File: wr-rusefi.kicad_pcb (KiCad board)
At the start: 2 copper layers, 94 x 94 mm, 147 parts, among them P101 USB_OTG, P102 CONN_01X08, P103 CONN_01X08, P104 CONN_01X04, P105 CONN_01X08, P106 CONN_01X08, P107 CONN_01X02, P108 USB_OTG, P109 CONN_01X02, P110 CONN_01X06, Q401 IRF540N, Q402 IRF540N, Q403 IRF540N, Q404 IRF540N, Q405 IRF540N, Q406 IRF540N, U101 ISL89410, U102 ISL89410, U103 FT230XS, U104 MAX9924, U105 MCP2562-E/SN, U106 LD1117S33TR, U107 MAX9924, U108 ISL89410, U109 STM32F407VGTx, U110 ISL89410, U201 LM324, U301 LM324, U501 LM7805CT, Y101 Crystal

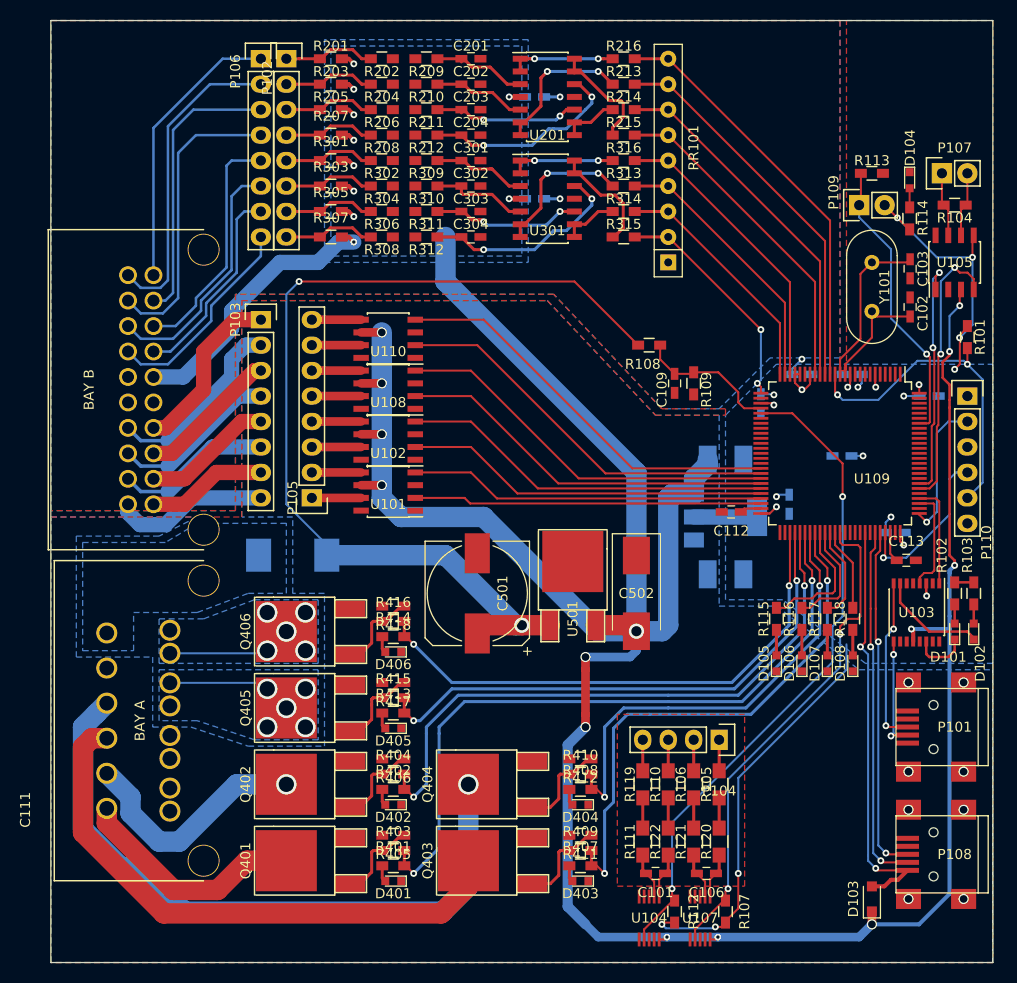
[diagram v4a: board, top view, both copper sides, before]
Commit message: Via stitching bonanza
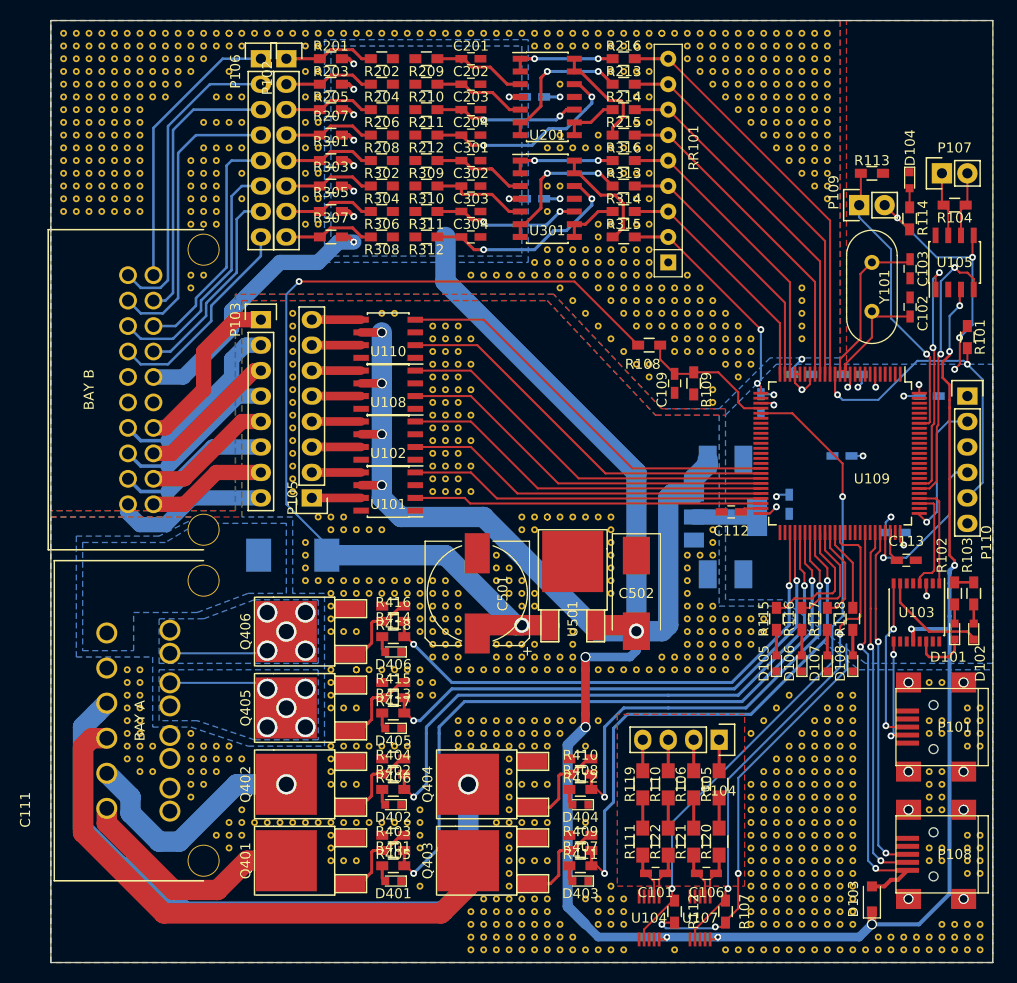
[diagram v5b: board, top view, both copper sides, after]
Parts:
- added REF**: via-stitch, wr-efi:via-stitch, F.Cu at (67.3, 132.1)
- added REF**: via-stitch, wr-efi:via-stitch, F.Cu at (139.7, 141.0)
- added REF**: via-stitch, wr-efi:via-stitch, F.Cu at (77.5, 55.9)
- added REF**: via-stitch, wr-efi:via-stitch, F.Cu at (62.2, 58.4)
- added REF**: via-stitch, wr-efi:via-stitch, F.Cu at (61.0, 52.1)
- added REF**: via-stitch, wr-efi:via-stitch, F.Cu at (61.0, 53.3)
- added REF**: via-stitch, wr-efi:via-stitch, F.Cu at (61.0, 54.6)
- added REF**: via-stitch, wr-efi:via-stitch, F.Cu at (61.0, 55.9)
- added REF**: via-stitch, wr-efi:via-stitch, F.Cu at (61.0, 57.1)
- added REF**: via-stitch, wr-efi:via-stitch, F.Cu at (61.0, 58.4)
- added REF**: via-stitch, wr-efi:via-stitch, F.Cu at (59.7, 69.8)
- added REF**: via-stitch, wr-efi:via-stitch, F.Cu at (58.4, 69.8)
- added REF**: via-stitch, wr-efi:via-stitch, F.Cu at (57.1, 69.8)
- added REF**: via-stitch, wr-efi:via-stitch, F.Cu at (77.5, 58.4)
- added REF**: via-stitch, wr-efi:via-stitch, F.Cu at (55.9, 69.8)
- added REF**: via-stitch, wr-efi:via-stitch, F.Cu at (54.6, 69.8)
- added REF**: via-stitch, wr-efi:via-stitch, F.Cu at (53.3, 69.8)
- added REF**: via-stitch, wr-efi:via-stitch, F.Cu at (52.1, 69.8)
- added REF**: via-stitch, wr-efi:via-stitch, F.Cu at (59.7, 68.6)
- added REF**: via-stitch, wr-efi:via-stitch, F.Cu at (58.4, 68.6)
- added REF**: via-stitch, wr-efi:via-stitch, F.Cu at (57.1, 68.6)
- added REF**: via-stitch, wr-efi:via-stitch, F.Cu at (55.9, 68.6)
- added REF**: via-stitch, wr-efi:via-stitch, F.Cu at (54.6, 68.6)
- added REF**: via-stitch, wr-efi:via-stitch, F.Cu at (53.3, 68.6)
- added REF**: via-stitch, wr-efi:via-stitch, F.Cu at (76.2, 58.4)
- added REF**: via-stitch, wr-efi:via-stitch, F.Cu at (52.1, 68.6)
- added REF**: via-stitch, wr-efi:via-stitch, F.Cu at (59.7, 67.3)
- added REF**: via-stitch, wr-efi:via-stitch, F.Cu at (58.4, 67.3)
- added REF**: via-stitch, wr-efi:via-stitch, F.Cu at (57.1, 67.3)
- added REF**: via-stitch, wr-efi:via-stitch, F.Cu at (55.9, 67.3)
- added REF**: via-stitch, wr-efi:via-stitch, F.Cu at (54.6, 67.3)
- added REF**: via-stitch, wr-efi:via-stitch, F.Cu at (53.3, 67.3)
- added REF**: via-stitch, wr-efi:via-stitch, F.Cu at (52.1, 67.3)
- added REF**: via-stitch, wr-efi:via-stitch, F.Cu at (59.7, 66.0)
- added REF**: via-stitch, wr-efi:via-stitch, F.Cu at (58.4, 66.0)
- added REF**: via-stitch, wr-efi:via-stitch, F.Cu at (76.2, 61.0)
- added REF**: via-stitch, wr-efi:via-stitch, F.Cu at (57.1, 66.0)
- added REF**: via-stitch, wr-efi:via-stitch, F.Cu at (55.9, 66.0)
- added REF**: via-stitch, wr-efi:via-stitch, F.Cu at (54.6, 66.0)
- added REF**: via-stitch, wr-efi:via-stitch, F.Cu at (53.3, 66.0)
- added REF**: via-stitch, wr-efi:via-stitch, F.Cu at (52.1, 66.0)
- added REF**: via-stitch, wr-efi:via-stitch, F.Cu at (59.7, 64.8)
- added REF**: via-stitch, wr-efi:via-stitch, F.Cu at (58.4, 64.8)
- added REF**: via-stitch, wr-efi:via-stitch, F.Cu at (57.1, 64.8)
- added REF**: via-stitch, wr-efi:via-stitch, F.Cu at (55.9, 64.8)
- added REF**: via-stitch, wr-efi:via-stitch, F.Cu at (54.6, 64.8)
- added REF**: via-stitch, wr-efi:via-stitch, F.Cu at (77.5, 61.0)
- added REF**: via-stitch, wr-efi:via-stitch, F.Cu at (53.3, 64.8)
- added REF**: via-stitch, wr-efi:via-stitch, F.Cu at (52.1, 64.8)
- added REF**: via-stitch, wr-efi:via-stitch, F.Cu at (59.7, 63.5)
- added REF**: via-stitch, wr-efi:via-stitch, F.Cu at (58.4, 63.5)
- added REF**: via-stitch, wr-efi:via-stitch, F.Cu at (57.1, 63.5)
- added REF**: via-stitch, wr-efi:via-stitch, F.Cu at (55.9, 63.5)
- added REF**: via-stitch, wr-efi:via-stitch, F.Cu at (54.6, 63.5)
- added REF**: via-stitch, wr-efi:via-stitch, F.Cu at (53.3, 63.5)
- added REF**: via-stitch, wr-efi:via-stitch, F.Cu at (52.1, 63.5)
- added REF**: via-stitch, wr-efi:via-stitch, F.Cu at (59.7, 62.2)
- added REF**: via-stitch, wr-efi:via-stitch, F.Cu at (77.5, 63.5)
- added REF**: via-stitch, wr-efi:via-stitch, F.Cu at (58.4, 62.2)
- added REF**: via-stitch, wr-efi:via-stitch, F.Cu at (57.1, 62.2)
- added REF**: via-stitch, wr-efi:via-stitch, F.Cu at (55.9, 62.2)
- added REF**: via-stitch, wr-efi:via-stitch, F.Cu at (54.6, 62.2)
- added REF**: via-stitch, wr-efi:via-stitch, F.Cu at (53.3, 62.2)
- added REF**: via-stitch, wr-efi:via-stitch, F.Cu at (52.1, 62.2)
- added REF**: via-stitch, wr-efi:via-stitch, F.Cu at (59.7, 61.0)
- added REF**: via-stitch, wr-efi:via-stitch, F.Cu at (58.4, 61.0)
- added REF**: via-stitch, wr-efi:via-stitch, F.Cu at (57.1, 61.0)
- added REF**: via-stitch, wr-efi:via-stitch, F.Cu at (55.9, 61.0)
- added REF**: via-stitch, wr-efi:via-stitch, F.Cu at (76.2, 63.5)
- added REF**: via-stitch, wr-efi:via-stitch, F.Cu at (54.6, 61.0)
- added REF**: via-stitch, wr-efi:via-stitch, F.Cu at (53.3, 61.0)
- added REF**: via-stitch, wr-efi:via-stitch, F.Cu at (52.1, 61.0)
- added REF**: via-stitch, wr-efi:via-stitch, F.Cu at (59.7, 59.7)
- added REF**: via-stitch, wr-efi:via-stitch, F.Cu at (58.4, 59.7)
- added REF**: via-stitch, wr-efi:via-stitch, F.Cu at (57.1, 59.7)
- added REF**: via-stitch, wr-efi:via-stitch, F.Cu at (55.9, 59.7)
- added REF**: via-stitch, wr-efi:via-stitch, F.Cu at (54.6, 59.7)
- added REF**: via-stitch, wr-efi:via-stitch, F.Cu at (53.3, 59.7)
- added REF**: via-stitch, wr-efi:via-stitch, F.Cu at (52.1, 59.7)
- added REF**: via-stitch, wr-efi:via-stitch, F.Cu at (77.5, 66.0)
- added REF**: via-stitch, wr-efi:via-stitch, F.Cu at (59.7, 58.4)
- added REF**: via-stitch, wr-efi:via-stitch, F.Cu at (58.4, 58.4)
- added REF**: via-stitch, wr-efi:via-stitch, F.Cu at (57.1, 58.4)
- added REF**: via-stitch, wr-efi:via-stitch, F.Cu at (55.9, 58.4)
- added REF**: via-stitch, wr-efi:via-stitch, F.Cu at (54.6, 58.4)
- added REF**: via-stitch, wr-efi:via-stitch, F.Cu at (53.3, 58.4)
- added REF**: via-stitch, wr-efi:via-stitch, F.Cu at (52.1, 58.4)
- added REF**: via-stitch, wr-efi:via-stitch, F.Cu at (59.7, 57.1)
- added REF**: via-stitch, wr-efi:via-stitch, F.Cu at (58.4, 57.1)
- added REF**: via-stitch, wr-efi:via-stitch, F.Cu at (57.1, 57.1)
- added REF**: via-stitch, wr-efi:via-stitch, F.Cu at (76.2, 66.0)
- added REF**: via-stitch, wr-efi:via-stitch, F.Cu at (55.9, 57.1)
- added REF**: via-stitch, wr-efi:via-stitch, F.Cu at (54.6, 57.1)
- added REF**: via-stitch, wr-efi:via-stitch, F.Cu at (53.3, 57.1)
- added REF**: via-stitch, wr-efi:via-stitch, F.Cu at (52.1, 57.1)
- added REF**: via-stitch, wr-efi:via-stitch, F.Cu at (59.7, 55.9)
- added REF**: via-stitch, wr-efi:via-stitch, F.Cu at (58.4, 55.9)
- added REF**: via-stitch, wr-efi:via-stitch, F.Cu at (57.1, 55.9)
- added REF**: via-stitch, wr-efi:via-stitch, F.Cu at (55.9, 55.9)
- added REF**: via-stitch, wr-efi:via-stitch, F.Cu at (54.6, 55.9)
- added REF**: via-stitch, wr-efi:via-stitch, F.Cu at (53.3, 55.9)
- added REF**: via-stitch, wr-efi:via-stitch, F.Cu at (76.2, 68.6)
- added REF**: via-stitch, wr-efi:via-stitch, F.Cu at (52.1, 55.9)
- added REF**: via-stitch, wr-efi:via-stitch, F.Cu at (59.7, 54.6)
- added REF**: via-stitch, wr-efi:via-stitch, F.Cu at (58.4, 54.6)
- added REF**: via-stitch, wr-efi:via-stitch, F.Cu at (57.1, 54.6)
- added REF**: via-stitch, wr-efi:via-stitch, F.Cu at (55.9, 54.6)
- added REF**: via-stitch, wr-efi:via-stitch, F.Cu at (54.6, 54.6)
- added REF**: via-stitch, wr-efi:via-stitch, F.Cu at (53.3, 54.6)
- added REF**: via-stitch, wr-efi:via-stitch, F.Cu at (52.1, 54.6)
- added REF**: via-stitch, wr-efi:via-stitch, F.Cu at (59.7, 53.3)
- added REF**: via-stitch, wr-efi:via-stitch, F.Cu at (58.4, 53.3)
- added REF**: via-stitch, wr-efi:via-stitch, F.Cu at (143.5, 141.0)
- added REF**: via-stitch, wr-efi:via-stitch, F.Cu at (77.5, 68.6)
- added REF**: via-stitch, wr-efi:via-stitch, F.Cu at (57.1, 53.3)
- added REF**: via-stitch, wr-efi:via-stitch, F.Cu at (55.9, 53.3)
- added REF**: via-stitch, wr-efi:via-stitch, F.Cu at (54.6, 53.3)
- added REF**: via-stitch, wr-efi:via-stitch, F.Cu at (53.3, 53.3)
- added REF**: via-stitch, wr-efi:via-stitch, F.Cu at (52.1, 53.3)
- added REF**: via-stitch, wr-efi:via-stitch, F.Cu at (59.7, 52.1)
- added REF**: via-stitch, wr-efi:via-stitch, F.Cu at (58.4, 52.1)
- added REF**: via-stitch, wr-efi:via-stitch, F.Cu at (57.1, 52.1)
- added REF**: via-stitch, wr-efi:via-stitch, F.Cu at (55.9, 52.1)
- added REF**: via-stitch, wr-efi:via-stitch, F.Cu at (54.6, 52.1)
- added REF**: via-stitch, wr-efi:via-stitch, F.Cu at (77.5, 71.1)
- added REF**: via-stitch, wr-efi:via-stitch, F.Cu at (53.3, 52.1)
- added REF**: via-stitch, wr-efi:via-stitch, F.Cu at (52.1, 52.1)
- added REF**: via-stitch, wr-efi:via-stitch, F.Cu at (76.2, 71.1)
- added REF**: via-stitch, wr-efi:via-stitch, F.Cu at (67.3, 71.1)
- added REF**: via-stitch, wr-efi:via-stitch, F.Cu at (66.0, 71.1)
- added REF**: via-stitch, wr-efi:via-stitch, F.Cu at (64.8, 71.1)
- added REF**: via-stitch, wr-efi:via-stitch, F.Cu at (69.8, 129.5)
- added REF**: via-stitch, wr-efi:via-stitch, F.Cu at (68.6, 130.8)
- added REF**: via-stitch, wr-efi:via-stitch, F.Cu at (61.0, 123.2)
- added REF**: via-stitch, wr-efi:via-stitch, F.Cu at (61.0, 125.7)
- added REF**: via-stitch, wr-efi:via-stitch, F.Cu at (143.5, 142.2)
- added REF**: via-stitch, wr-efi:via-stitch, F.Cu at (64.8, 121.9)
- added REF**: via-stitch, wr-efi:via-stitch, F.Cu at (78.7, 101.6)
- added REF**: via-stitch, wr-efi:via-stitch, F.Cu at (77.5, 100.3)
- added REF**: via-stitch, wr-efi:via-stitch, F.Cu at (74.9, 97.8)
- added REF**: via-stitch, wr-efi:via-stitch, F.Cu at (74.9, 96.5)
- added REF**: via-stitch, wr-efi:via-stitch, F.Cu at (74.9, 95.2)
- added REF**: via-stitch, wr-efi:via-stitch, F.Cu at (74.9, 94.0)
- added REF**: via-stitch, wr-efi:via-stitch, F.Cu at (74.9, 92.7)
- added REF**: via-stitch, wr-efi:via-stitch, F.Cu at (74.9, 91.4)
- added REF**: via-stitch, wr-efi:via-stitch, F.Cu at (74.9, 90.2)
- added REF**: via-stitch, wr-efi:via-stitch, F.Cu at (143.5, 143.5)
- added REF**: via-stitch, wr-efi:via-stitch, F.Cu at (74.9, 88.9)
- added REF**: via-stitch, wr-efi:via-stitch, F.Cu at (74.9, 87.6)
- added REF**: via-stitch, wr-efi:via-stitch, F.Cu at (74.9, 86.4)
- added REF**: via-stitch, wr-efi:via-stitch, F.Cu at (74.9, 85.1)
- added REF**: via-stitch, wr-efi:via-stitch, F.Cu at (74.9, 83.8)
- added REF**: via-stitch, wr-efi:via-stitch, F.Cu at (74.9, 82.5)
- added REF**: via-stitch, wr-efi:via-stitch, F.Cu at (83.8, 80.0)
- added REF**: via-stitch, wr-efi:via-stitch, F.Cu at (85.1, 80.0)
- added REF**: via-stitch, wr-efi:via-stitch, F.Cu at (125.7, 77.5)
- added REF**: via-stitch, wr-efi:via-stitch, F.Cu at (125.7, 78.7)
- added REF**: via-stitch, wr-efi:via-stitch, F.Cu at (139.7, 143.5)
- added REF**: via-stitch, wr-efi:via-stitch, F.Cu at (125.7, 80.0)
- added REF**: via-stitch, wr-efi:via-stitch, F.Cu at (125.7, 81.3)
- added REF**: via-stitch, wr-efi:via-stitch, F.Cu at (125.7, 82.5)
- added REF**: via-stitch, wr-efi:via-stitch, F.Cu at (64.8, 77.5)
- added REF**: via-stitch, wr-efi:via-stitch, F.Cu at (64.8, 76.2)
- added REF**: via-stitch, wr-efi:via-stitch, F.Cu at (68.6, 55.9)
- added REF**: via-stitch, wr-efi:via-stitch, F.Cu at (67.3, 58.4)
- added REF**: via-stitch, wr-efi:via-stitch, F.Cu at (68.6, 58.4)
- added REF**: via-stitch, wr-efi:via-stitch, F.Cu at (69.8, 58.4)
- added REF**: via-stitch, wr-efi:via-stitch, F.Cu at (69.8, 68.6)
- added REF**: via-stitch, wr-efi:via-stitch, F.Cu at (141.0, 143.5)
- added REF**: via-stitch, wr-efi:via-stitch, F.Cu at (69.8, 66.0)
- added REF**: via-stitch, wr-efi:via-stitch, F.Cu at (66.0, 66.0)
- added REF**: via-stitch, wr-efi:via-stitch, F.Cu at (67.3, 66.0)
- added REF**: via-stitch, wr-efi:via-stitch, F.Cu at (67.3, 67.3)
- added REF**: via-stitch, wr-efi:via-stitch, F.Cu at (66.0, 67.3)
- added REF**: via-stitch, wr-efi:via-stitch, F.Cu at (66.0, 68.6)
- added REF**: via-stitch, wr-efi:via-stitch, F.Cu at (67.3, 68.6)
- added REF**: via-stitch, wr-efi:via-stitch, F.Cu at (67.3, 69.8)
- added REF**: via-stitch, wr-efi:via-stitch, F.Cu at (66.0, 69.8)
- added REF**: via-stitch, wr-efi:via-stitch, F.Cu at (64.8, 69.8)
- added REF**: via-stitch, wr-efi:via-stitch, F.Cu at (142.2, 143.5)
- added REF**: via-stitch, wr-efi:via-stitch, F.Cu at (64.8, 68.6)
- added REF**: via-stitch, wr-efi:via-stitch, F.Cu at (64.8, 67.3)
- added REF**: via-stitch, wr-efi:via-stitch, F.Cu at (64.8, 66.0)
- added REF**: via-stitch, wr-efi:via-stitch, F.Cu at (67.3, 64.8)
- added REF**: via-stitch, wr-efi:via-stitch, F.Cu at (66.0, 64.8)
- added REF**: via-stitch, wr-efi:via-stitch, F.Cu at (64.8, 64.8)
- added REF**: via-stitch, wr-efi:via-stitch, F.Cu at (66.0, 63.5)
- added REF**: via-stitch, wr-efi:via-stitch, F.Cu at (67.3, 63.5)
- added REF**: via-stitch, wr-efi:via-stitch, F.Cu at (68.6, 63.5)
- added REF**: via-stitch, wr-efi:via-stitch, F.Cu at (67.3, 61.0)
- added REF**: via-stitch, wr-efi:via-stitch, F.Cu at (137.2, 143.5)
- added REF**: via-stitch, wr-efi:via-stitch, F.Cu at (66.0, 61.0)
- added REF**: via-stitch, wr-efi:via-stitch, F.Cu at (68.6, 61.0)
- added REF**: via-stitch, wr-efi:via-stitch, F.Cu at (69.8, 61.0)
- added REF**: via-stitch, wr-efi:via-stitch, F.Cu at (69.8, 63.5)
- added REF**: via-stitch, wr-efi:via-stitch, F.Cu at (101.6, 62.2)
- added REF**: via-stitch, wr-efi:via-stitch, F.Cu at (101.6, 57.1)
- added REF**: via-stitch, wr-efi:via-stitch, F.Cu at (100.3, 69.8)
- added REF**: via-stitch, wr-efi:via-stitch, F.Cu at (100.3, 67.3)
- added REF**: via-stitch, wr-efi:via-stitch, F.Cu at (101.6, 67.3)
- added REF**: via-stitch, wr-efi:via-stitch, F.Cu at (105.4, 72.4)
- added REF**: via-stitch, wr-efi:via-stitch, F.Cu at (138.4, 143.5)
- added REF**: via-stitch, wr-efi:via-stitch, F.Cu at (105.4, 71.1)
- added REF**: via-stitch, wr-efi:via-stitch, F.Cu at (106.7, 71.1)
- added REF**: via-stitch, wr-efi:via-stitch, F.Cu at (109.2, 71.1)
- added REF**: via-stitch, wr-efi:via-stitch, F.Cu at (110.5, 71.1)
- added REF**: via-stitch, wr-efi:via-stitch, F.Cu at (109.2, 68.6)
- added REF**: via-stitch, wr-efi:via-stitch, F.Cu at (110.5, 68.6)
- added REF**: via-stitch, wr-efi:via-stitch, F.Cu at (110.5, 66.0)
- added REF**: via-stitch, wr-efi:via-stitch, F.Cu at (109.2, 66.0)
- added REF**: via-stitch, wr-efi:via-stitch, F.Cu at (108.0, 66.0)
- added REF**: via-stitch, wr-efi:via-stitch, F.Cu at (106.7, 66.0)
- added REF**: via-stitch, wr-efi:via-stitch, F.Cu at (135.9, 143.5)
- added REF**: via-stitch, wr-efi:via-stitch, F.Cu at (106.7, 55.9)
- added REF**: via-stitch, wr-efi:via-stitch, F.Cu at (108.0, 55.9)
- added REF**: via-stitch, wr-efi:via-stitch, F.Cu at (109.2, 55.9)
- added REF**: via-stitch, wr-efi:via-stitch, F.Cu at (110.5, 55.9)
- added REF**: via-stitch, wr-efi:via-stitch, F.Cu at (110.5, 58.4)
- added REF**: via-stitch, wr-efi:via-stitch, F.Cu at (109.2, 58.4)
- added REF**: via-stitch, wr-efi:via-stitch, F.Cu at (109.2, 61.0)
- added REF**: via-stitch, wr-efi:via-stitch, F.Cu at (110.5, 61.0)
- added REF**: via-stitch, wr-efi:via-stitch, F.Cu at (110.5, 63.5)
- added REF**: via-stitch, wr-efi:via-stitch, F.Cu at (109.2, 63.5)
- added REF**: via-stitch, wr-efi:via-stitch, F.Cu at (66.0, 76.2)
- added REF**: via-stitch, wr-efi:via-stitch, F.Cu at (134.6, 143.5)
- added REF**: via-stitch, wr-efi:via-stitch, F.Cu at (108.0, 63.5)
- added REF**: via-stitch, wr-efi:via-stitch, F.Cu at (106.7, 63.5)
- added REF**: via-stitch, wr-efi:via-stitch, F.Cu at (105.4, 62.2)
- added REF**: via-stitch, wr-efi:via-stitch, F.Cu at (105.4, 63.5)
- added REF**: via-stitch, wr-efi:via-stitch, F.Cu at (104.1, 63.5)
- added REF**: via-stitch, wr-efi:via-stitch, F.Cu at (102.9, 63.5)
- added REF**: via-stitch, wr-efi:via-stitch, F.Cu at (101.6, 63.5)
- added REF**: via-stitch, wr-efi:via-stitch, F.Cu at (100.3, 63.5)
- added REF**: via-stitch, wr-efi:via-stitch, F.Cu at (69.8, 53.3)
- added REF**: via-stitch, wr-efi:via-stitch, F.Cu at (77.5, 53.3)
- added REF**: via-stitch, wr-efi:via-stitch, F.Cu at (133.3, 143.5)
- added REF**: via-stitch, wr-efi:via-stitch, F.Cu at (76.2, 53.3)
- added REF**: via-stitch, wr-efi:via-stitch, F.Cu at (97.8, 52.1)
- added REF**: via-stitch, wr-efi:via-stitch, F.Cu at (96.5, 52.1)
- added REF**: via-stitch, wr-efi:via-stitch, F.Cu at (95.2, 52.1)
- added REF**: via-stitch, wr-efi:via-stitch, F.Cu at (94.0, 52.1)
- added REF**: via-stitch, wr-efi:via-stitch, F.Cu at (92.7, 52.1)
- added REF**: via-stitch, wr-efi:via-stitch, F.Cu at (91.4, 52.1)
- added REF**: via-stitch, wr-efi:via-stitch, F.Cu at (90.2, 52.1)
- added REF**: via-stitch, wr-efi:via-stitch, F.Cu at (88.9, 52.1)
- added REF**: via-stitch, wr-efi:via-stitch, F.Cu at (87.6, 52.1)
- added REF**: via-stitch, wr-efi:via-stitch, F.Cu at (132.1, 143.5)
- added REF**: via-stitch, wr-efi:via-stitch, F.Cu at (86.4, 52.1)
- added REF**: via-stitch, wr-efi:via-stitch, F.Cu at (85.1, 52.1)
- added REF**: via-stitch, wr-efi:via-stitch, F.Cu at (83.8, 52.1)
- added REF**: via-stitch, wr-efi:via-stitch, F.Cu at (82.5, 52.1)
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
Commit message: more vias
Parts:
- added REF**: via-stitch, wr-efi:via-stitch, F.Cu at (105.4, 137.2)
- added REF**: via-stitch, wr-efi:via-stitch, F.Cu at (111.8, 88.9)
- added REF**: via-stitch, wr-efi:via-stitch, F.Cu at (113.0, 91.4)
- added REF**: via-stitch, wr-efi:via-stitch, F.Cu at (111.8, 91.4)
- added REF**: via-stitch, wr-efi:via-stitch, F.Cu at (111.8, 92.7)
- added REF**: via-stitch, wr-efi:via-stitch, F.Cu at (106.7, 90.2)
- added REF**: via-stitch, wr-efi:via-stitch, F.Cu at (105.4, 88.9)
- added REF**: via-stitch, wr-efi:via-stitch, F.Cu at (104.1, 87.6)
- added REF**: via-stitch, wr-efi:via-stitch, F.Cu at (102.9, 86.4)
- added REF**: via-stitch, wr-efi:via-stitch, F.Cu at (101.6, 85.1)
- added REF**: via-stitch, wr-efi:via-stitch, F.Cu at (100.3, 83.8)
- added REF**: via-stitch, wr-efi:via-stitch, F.Cu at (99.1, 82.5)
- added REF**: via-stitch, wr-efi:via-stitch, F.Cu at (111.8, 87.6)
- added REF**: via-stitch, wr-efi:via-stitch, F.Cu at (106.7, 91.4)
- added REF**: via-stitch, wr-efi:via-stitch, F.Cu at (105.4, 90.2)
- added REF**: via-stitch, wr-efi:via-stitch, F.Cu at (104.1, 88.9)
- added REF**: via-stitch, wr-efi:via-stitch, F.Cu at (102.9, 87.6)
- added REF**: via-stitch, wr-efi:via-stitch, F.Cu at (101.6, 86.4)
- added REF**: via-stitch, wr-efi:via-stitch, F.Cu at (100.3, 85.1)
- added REF**: via-stitch, wr-efi:via-stitch, F.Cu at (99.1, 83.8)
- added REF**: via-stitch, wr-efi:via-stitch, F.Cu at (97.8, 82.5)
- added REF**: via-stitch, wr-efi:via-stitch, F.Cu at (61.0, 121.9)
- added REF**: via-stitch, wr-efi:via-stitch, F.Cu at (61.0, 124.5)
- added REF**: via-stitch, wr-efi:via-stitch, F.Cu at (111.8, 86.4)
- added REF**: via-stitch, wr-efi:via-stitch, F.Cu at (61.0, 128.3)
- added REF**: via-stitch, wr-efi:via-stitch, F.Cu at (61.0, 127.0)
- added REF**: via-stitch, wr-efi:via-stitch, F.Cu at (53.3, 119.4)
- added REF**: via-stitch, wr-efi:via-stitch, F.Cu at (52.1, 114.3)
- added REF**: via-stitch, wr-efi:via-stitch, F.Cu at (52.1, 113.0)
- added REF**: via-stitch, wr-efi:via-stitch, F.Cu at (52.1, 110.5)
- added REF**: via-stitch, wr-efi:via-stitch, F.Cu at (52.1, 111.8)
- added REF**: via-stitch, wr-efi:via-stitch, F.Cu at (52.1, 109.2)
- added REF**: via-stitch, wr-efi:via-stitch, F.Cu at (52.1, 108.0)
- added REF**: via-stitch, wr-efi:via-stitch, F.Cu at (52.1, 106.7)
- added REF**: via-stitch, wr-efi:via-stitch, F.Cu at (52.1, 72.4)
- added REF**: via-stitch, wr-efi:via-stitch, F.Cu at (52.1, 105.4)
- added REF**: via-stitch, wr-efi:via-stitch, F.Cu at (52.1, 104.1)
- added REF**: via-stitch, wr-efi:via-stitch, F.Cu at (52.1, 102.9)
- added REF**: via-stitch, wr-efi:via-stitch, F.Cu at (52.1, 101.6)
- added REF**: via-stitch, wr-efi:via-stitch, F.Cu at (54.6, 101.6)
- added REF**: via-stitch, wr-efi:via-stitch, F.Cu at (53.3, 101.6)
- added REF**: via-stitch, wr-efi:via-stitch, F.Cu at (55.9, 101.6)
- added REF**: via-stitch, wr-efi:via-stitch, F.Cu at (57.1, 101.6)
- added REF**: via-stitch, wr-efi:via-stitch, F.Cu at (54.6, 115.6)
- added REF**: via-stitch, wr-efi:via-stitch, F.Cu at (53.3, 115.6)
- added REF**: via-stitch, wr-efi:via-stitch, F.Cu at (126.4, 72.4)
- added REF**: via-stitch, wr-efi:via-stitch, F.Cu at (52.1, 115.6)
- added REF**: via-stitch, wr-efi:via-stitch, F.Cu at (52.1, 118.1)
- added REF**: via-stitch, wr-efi:via-stitch, F.Cu at (52.1, 116.8)
- added REF**: via-stitch, wr-efi:via-stitch, F.Cu at (53.3, 116.8)
- added REF**: via-stitch, wr-efi:via-stitch, F.Cu at (54.6, 116.8)
- added REF**: via-stitch, wr-efi:via-stitch, F.Cu at (53.3, 118.1)
- added REF**: via-stitch, wr-efi:via-stitch, F.Cu at (52.1, 132.1)
- added REF**: via-stitch, wr-efi:via-stitch, F.Cu at (52.1, 130.8)
- added REF**: via-stitch, wr-efi:via-stitch, F.Cu at (52.1, 129.5)
- added REF**: via-stitch, wr-efi:via-stitch, F.Cu at (52.1, 128.3)
- added REF**: via-stitch, wr-efi:via-stitch, F.Cu at (116.2, 62.2)
- added REF**: via-stitch, wr-efi:via-stitch, F.Cu at (52.1, 127.0)
- added REF**: via-stitch, wr-efi:via-stitch, F.Cu at (52.1, 123.2)
- added REF**: via-stitch, wr-efi:via-stitch, F.Cu at (52.1, 125.7)
- added REF**: via-stitch, wr-efi:via-stitch, F.Cu at (52.1, 124.5)
- added REF**: via-stitch, wr-efi:via-stitch, F.Cu at (52.1, 121.9)
- added REF**: via-stitch, wr-efi:via-stitch, F.Cu at (52.1, 120.7)
- added REF**: via-stitch, wr-efi:via-stitch, F.Cu at (52.1, 119.4)
- added REF**: via-stitch, wr-efi:via-stitch, F.Cu at (54.6, 139.7)
- added REF**: via-stitch, wr-efi:via-stitch, F.Cu at (57.1, 139.7)
- added REF**: via-stitch, wr-efi:via-stitch, F.Cu at (55.9, 139.7)
- added REF**: via-stitch, wr-efi:via-stitch, F.Cu at (117.5, 63.5)
- added REF**: via-stitch, wr-efi:via-stitch, F.Cu at (55.9, 138.4)
- added REF**: via-stitch, wr-efi:via-stitch, F.Cu at (54.6, 138.4)
- added REF**: via-stitch, wr-efi:via-stitch, F.Cu at (54.6, 137.2)
- added REF**: via-stitch, wr-efi:via-stitch, F.Cu at (53.3, 135.9)
- added REF**: via-stitch, wr-efi:via-stitch, F.Cu at (53.3, 137.2)
- added REF**: via-stitch, wr-efi:via-stitch, F.Cu at (53.3, 138.4)
- added REF**: via-stitch, wr-efi:via-stitch, F.Cu at (53.3, 139.7)
- added REF**: via-stitch, wr-efi:via-stitch, F.Cu at (53.3, 141.0)
- added REF**: via-stitch, wr-efi:via-stitch, F.Cu at (54.6, 141.0)
- added REF**: via-stitch, wr-efi:via-stitch, F.Cu at (55.9, 141.0)
- added REF**: via-stitch, wr-efi:via-stitch, F.Cu at (118.7, 64.8)
- added REF**: via-stitch, wr-efi:via-stitch, F.Cu at (57.1, 141.0)
- added REF**: via-stitch, wr-efi:via-stitch, F.Cu at (58.4, 141.0)
- added REF**: via-stitch, wr-efi:via-stitch, F.Cu at (59.7, 141.0)
- added REF**: via-stitch, wr-efi:via-stitch, F.Cu at (58.4, 139.7)
- added REF**: via-stitch, wr-efi:via-stitch, F.Cu at (57.1, 138.4)
- added REF**: via-stitch, wr-efi:via-stitch, F.Cu at (55.9, 137.2)
- added REF**: via-stitch, wr-efi:via-stitch, F.Cu at (54.6, 135.9)
- added REF**: via-stitch, wr-efi:via-stitch, F.Cu at (53.3, 134.6)
- added REF**: via-stitch, wr-efi:via-stitch, F.Cu at (52.1, 133.3)
- added REF**: via-stitch, wr-efi:via-stitch, F.Cu at (52.1, 134.6)
- added REF**: via-stitch, wr-efi:via-stitch, F.Cu at (120.0, 66.0)
- added REF**: via-stitch, wr-efi:via-stitch, F.Cu at (52.1, 135.9)
- added REF**: via-stitch, wr-efi:via-stitch, F.Cu at (52.1, 137.2)
- added REF**: via-stitch, wr-efi:via-stitch, F.Cu at (52.1, 138.4)
- added REF**: via-stitch, wr-efi:via-stitch, F.Cu at (52.1, 139.7)
- added REF**: via-stitch, wr-efi:via-stitch, F.Cu at (52.1, 141.0)
- added REF**: via-stitch, wr-efi:via-stitch, F.Cu at (91.4, 143.5)
- added REF**: via-stitch, wr-efi:via-stitch, F.Cu at (91.4, 141.0)
- added REF**: via-stitch, wr-efi:via-stitch, F.Cu at (91.4, 142.2)
- added REF**: via-stitch, wr-efi:via-stitch, F.Cu at (90.2, 143.5)
- added REF**: via-stitch, wr-efi:via-stitch, F.Cu at (88.9, 143.5)
- added REF**: via-stitch, wr-efi:via-stitch, F.Cu at (121.3, 67.3)
- added REF**: via-stitch, wr-efi:via-stitch, F.Cu at (87.6, 143.5)
- added REF**: via-stitch, wr-efi:via-stitch, F.Cu at (86.4, 143.5)
- added REF**: via-stitch, wr-efi:via-stitch, F.Cu at (85.1, 143.5)
- added REF**: via-stitch, wr-efi:via-stitch, F.Cu at (83.8, 143.5)
- added REF**: via-stitch, wr-efi:via-stitch, F.Cu at (82.5, 143.5)
- added REF**: via-stitch, wr-efi:via-stitch, F.Cu at (81.3, 143.5)
- added REF**: via-stitch, wr-efi:via-stitch, F.Cu at (80.0, 143.5)
- added REF**: via-stitch, wr-efi:via-stitch, F.Cu at (78.7, 143.5)
- added REF**: via-stitch, wr-efi:via-stitch, F.Cu at (77.5, 143.5)
- added REF**: via-stitch, wr-efi:via-stitch, F.Cu at (76.2, 143.5)
- added REF**: via-stitch, wr-efi:via-stitch, F.Cu at (109.2, 141.0)
- added REF**: via-stitch, wr-efi:via-stitch, F.Cu at (122.6, 68.6)
- added REF**: via-stitch, wr-efi:via-stitch, F.Cu at (90.2, 142.2)
- added REF**: via-stitch, wr-efi:via-stitch, F.Cu at (88.9, 142.2)
- added REF**: via-stitch, wr-efi:via-stitch, F.Cu at (87.6, 142.2)
- added REF**: via-stitch, wr-efi:via-stitch, F.Cu at (86.4, 142.2)
- added REF**: via-stitch, wr-efi:via-stitch, F.Cu at (85.1, 142.2)
- added REF**: via-stitch, wr-efi:via-stitch, F.Cu at (83.8, 142.2)
- added REF**: via-stitch, wr-efi:via-stitch, F.Cu at (82.5, 142.2)
- added REF**: via-stitch, wr-efi:via-stitch, F.Cu at (81.3, 142.2)
- added REF**: via-stitch, wr-efi:via-stitch, F.Cu at (80.0, 142.2)
- added REF**: via-stitch, wr-efi:via-stitch, F.Cu at (78.7, 142.2)
- added REF**: via-stitch, wr-efi:via-stitch, F.Cu at (123.8, 69.8)
- added REF**: via-stitch, wr-efi:via-stitch, F.Cu at (77.5, 142.2)
- added REF**: via-stitch, wr-efi:via-stitch, F.Cu at (74.9, 143.5)
- added REF**: via-stitch, wr-efi:via-stitch, F.Cu at (73.7, 143.5)
- added REF**: via-stitch, wr-efi:via-stitch, F.Cu at (72.4, 143.5)
- added REF**: via-stitch, wr-efi:via-stitch, F.Cu at (71.1, 143.5)
- added REF**: via-stitch, wr-efi:via-stitch, F.Cu at (69.8, 143.5)
- added REF**: via-stitch, wr-efi:via-stitch, F.Cu at (68.6, 143.5)
- added REF**: via-stitch, wr-efi:via-stitch, F.Cu at (67.3, 143.5)
- added REF**: via-stitch, wr-efi:via-stitch, F.Cu at (66.0, 143.5)
- added REF**: via-stitch, wr-efi:via-stitch, F.Cu at (64.8, 143.5)
- added REF**: via-stitch, wr-efi:via-stitch, F.Cu at (125.1, 71.1)
- added REF**: via-stitch, wr-efi:via-stitch, F.Cu at (63.5, 143.5)
- added REF**: via-stitch, wr-efi:via-stitch, F.Cu at (62.2, 143.5)
- added REF**: via-stitch, wr-efi:via-stitch, F.Cu at (61.0, 143.5)
- added REF**: via-stitch, wr-efi:via-stitch, F.Cu at (59.7, 143.5)
- added REF**: via-stitch, wr-efi:via-stitch, F.Cu at (58.4, 143.5)
- added REF**: via-stitch, wr-efi:via-stitch, F.Cu at (57.1, 143.5)
- added REF**: via-stitch, wr-efi:via-stitch, F.Cu at (55.9, 143.5)
- added REF**: via-stitch, wr-efi:via-stitch, F.Cu at (54.6, 143.5)
- added REF**: via-stitch, wr-efi:via-stitch, F.Cu at (53.3, 143.5)
- added REF**: via-stitch, wr-efi:via-stitch, F.Cu at (52.1, 143.5)
- added REF**: via-stitch, wr-efi:via-stitch, F.Cu at (127.6, 71.1)
- added REF**: via-stitch, wr-efi:via-stitch, F.Cu at (76.2, 142.2)
- added REF**: via-stitch, wr-efi:via-stitch, F.Cu at (74.9, 142.2)
- added REF**: via-stitch, wr-efi:via-stitch, F.Cu at (73.7, 142.2)
- added REF**: via-stitch, wr-efi:via-stitch, F.Cu at (72.4, 142.2)
- added REF**: via-stitch, wr-efi:via-stitch, F.Cu at (71.1, 142.2)
- added REF**: via-stitch, wr-efi:via-stitch, F.Cu at (69.8, 142.2)
- added REF**: via-stitch, wr-efi:via-stitch, F.Cu at (68.6, 142.2)
- added REF**: via-stitch, wr-efi:via-stitch, F.Cu at (67.3, 142.2)
- added REF**: via-stitch, wr-efi:via-stitch, F.Cu at (66.0, 142.2)
- added REF**: via-stitch, wr-efi:via-stitch, F.Cu at (64.8, 142.2)
- added REF**: via-stitch, wr-efi:via-stitch, F.Cu at (126.4, 69.8)
- added REF**: via-stitch, wr-efi:via-stitch, F.Cu at (63.5, 142.2)
- added REF**: via-stitch, wr-efi:via-stitch, F.Cu at (62.2, 142.2)
- added REF**: via-stitch, wr-efi:via-stitch, F.Cu at (61.0, 142.2)
- added REF**: via-stitch, wr-efi:via-stitch, F.Cu at (59.7, 142.2)
- added REF**: via-stitch, wr-efi:via-stitch, F.Cu at (58.4, 142.2)
- added REF**: via-stitch, wr-efi:via-stitch, F.Cu at (57.1, 142.2)
- added REF**: via-stitch, wr-efi:via-stitch, F.Cu at (55.9, 142.2)
- added REF**: via-stitch, wr-efi:via-stitch, F.Cu at (54.6, 142.2)
- added REF**: via-stitch, wr-efi:via-stitch, F.Cu at (53.3, 142.2)
- added REF**: via-stitch, wr-efi:via-stitch, F.Cu at (52.1, 142.2)
- added REF**: via-stitch, wr-efi:via-stitch, F.Cu at (125.1, 68.6)
- added REF**: via-stitch, wr-efi:via-stitch, F.Cu at (138.4, 138.4)
- added REF**: via-stitch, wr-efi:via-stitch, F.Cu at (133.3, 138.4)
- added REF**: via-stitch, wr-efi:via-stitch, F.Cu at (132.1, 138.4)
- added REF**: via-stitch, wr-efi:via-stitch, F.Cu at (130.8, 116.8)
- added REF**: via-stitch, wr-efi:via-stitch, F.Cu at (127.0, 115.6)
- added REF**: via-stitch, wr-efi:via-stitch, F.Cu at (125.7, 116.8)
- added REF**: via-stitch, wr-efi:via-stitch, F.Cu at (125.7, 83.8)
- added REF**: via-stitch, wr-efi:via-stitch, F.Cu at (63.5, 80.0)
- added REF**: via-stitch, wr-efi:via-stitch, F.Cu at (57.1, 97.8)
- added REF**: via-stitch, wr-efi:via-stitch, F.Cu at (57.1, 95.2)
- added REF**: via-stitch, wr-efi:via-stitch, F.Cu at (123.8, 67.3)
- added REF**: via-stitch, wr-efi:via-stitch, F.Cu at (57.1, 92.7)
- added REF**: via-stitch, wr-efi:via-stitch, F.Cu at (57.1, 90.2)
- added REF**: via-stitch, wr-efi:via-stitch, F.Cu at (57.1, 87.6)
- added REF**: via-stitch, wr-efi:via-stitch, F.Cu at (57.1, 85.1)
- added REF**: via-stitch, wr-efi:via-stitch, F.Cu at (57.1, 82.5)
- added REF**: via-stitch, wr-efi:via-stitch, F.Cu at (57.1, 77.5)
- added REF**: via-stitch, wr-efi:via-stitch, F.Cu at (57.1, 73.7)
- added REF**: via-stitch, wr-efi:via-stitch, F.Cu at (58.4, 73.7)
- added REF**: via-stitch, wr-efi:via-stitch, F.Cu at (59.7, 73.7)
- added REF**: via-stitch, wr-efi:via-stitch, F.Cu at (59.7, 72.4)
- added REF**: via-stitch, wr-efi:via-stitch, F.Cu at (122.6, 66.0)
- added REF**: via-stitch, wr-efi:via-stitch, F.Cu at (58.4, 72.4)
- added REF**: via-stitch, wr-efi:via-stitch, F.Cu at (55.9, 99.1)
- added REF**: via-stitch, wr-efi:via-stitch, F.Cu at (54.6, 99.1)
- added REF**: via-stitch, wr-efi:via-stitch, F.Cu at (53.3, 99.1)
- added REF**: via-stitch, wr-efi:via-stitch, F.Cu at (52.1, 99.1)
- added REF**: via-stitch, wr-efi:via-stitch, F.Cu at (55.9, 97.8)
- added REF**: via-stitch, wr-efi:via-stitch, F.Cu at (54.6, 97.8)
- added REF**: via-stitch, wr-efi:via-stitch, F.Cu at (53.3, 97.8)
- added REF**: via-stitch, wr-efi:via-stitch, F.Cu at (52.1, 97.8)
- added REF**: via-stitch, wr-efi:via-stitch, F.Cu at (55.9, 96.5)
- added REF**: via-stitch, wr-efi:via-stitch, F.Cu at (121.3, 64.8)
- added REF**: via-stitch, wr-efi:via-stitch, F.Cu at (54.6, 96.5)
- added REF**: via-stitch, wr-efi:via-stitch, F.Cu at (53.3, 96.5)
- added REF**: via-stitch, wr-efi:via-stitch, F.Cu at (52.1, 96.5)
- added REF**: via-stitch, wr-efi:via-stitch, F.Cu at (55.9, 95.2)
- added REF**: via-stitch, wr-efi:via-stitch, F.Cu at (54.6, 95.2)
- added REF**: via-stitch, wr-efi:via-stitch, F.Cu at (53.3, 95.2)
- added REF**: via-stitch, wr-efi:via-stitch, F.Cu at (52.1, 95.2)
- added REF**: via-stitch, wr-efi:via-stitch, F.Cu at (55.9, 94.0)
- added REF**: via-stitch, wr-efi:via-stitch, F.Cu at (54.6, 94.0)
- added REF**: via-stitch, wr-efi:via-stitch, F.Cu at (53.3, 94.0)
- added REF**: via-stitch, wr-efi:via-stitch, F.Cu at (120.0, 63.5)
- added REF**: via-stitch, wr-efi:via-stitch, F.Cu at (52.1, 94.0)
- added REF**: via-stitch, wr-efi:via-stitch, F.Cu at (55.9, 92.7)
- added REF**: via-stitch, wr-efi:via-stitch, F.Cu at (54.6, 92.7)
- added REF**: via-stitch, wr-efi:via-stitch, F.Cu at (53.3, 92.7)
- added REF**: via-stitch, wr-efi:via-stitch, F.Cu at (52.1, 92.7)
- added REF**: via-stitch, wr-efi:via-stitch, F.Cu at (55.9, 91.4)
- added REF**: via-stitch, wr-efi:via-stitch, F.Cu at (54.6, 91.4)
- added REF**: via-stitch, wr-efi:via-stitch, F.Cu at (53.3, 91.4)
- added REF**: via-stitch, wr-efi:via-stitch, F.Cu at (52.1, 91.4)
- added REF**: via-stitch, wr-efi:via-stitch, F.Cu at (55.9, 90.2)
- added REF**: via-stitch, wr-efi:via-stitch, F.Cu at (109.2, 139.7)
- added REF**: via-stitch, wr-efi:via-stitch, F.Cu at (118.7, 62.2)
- added REF**: via-stitch, wr-efi:via-stitch, F.Cu at (54.6, 90.2)
- added REF**: via-stitch, wr-efi:via-stitch, F.Cu at (53.3, 90.2)
- added REF**: via-stitch, wr-efi:via-stitch, F.Cu at (52.1, 90.2)
- added REF**: via-stitch, wr-efi:via-stitch, F.Cu at (55.9, 88.9)
- added REF**: via-stitch, wr-efi:via-stitch, F.Cu at (54.6, 88.9)
- added REF**: via-stitch, wr-efi:via-stitch, F.Cu at (53.3, 88.9)
- added REF**: via-stitch, wr-efi:via-stitch, F.Cu at (52.1, 88.9)
- added REF**: via-stitch, wr-efi:via-stitch, F.Cu at (55.9, 87.6)
- added REF**: via-stitch, wr-efi:via-stitch, F.Cu at (54.6, 87.6)
- added REF**: via-stitch, wr-efi:via-stitch, F.Cu at (53.3, 87.6)
- added REF**: via-stitch, wr-efi:via-stitch, F.Cu at (117.5, 61.0)
- added REF**: via-stitch, wr-efi:via-stitch, F.Cu at (52.1, 87.6)
- added REF**: via-stitch, wr-efi:via-stitch, F.Cu at (55.9, 86.4)
- added REF**: via-stitch, wr-efi:via-stitch, F.Cu at (54.6, 86.4)
- added REF**: via-stitch, wr-efi:via-stitch, F.Cu at (53.3, 86.4)
- added REF**: via-stitch, wr-efi:via-stitch, F.Cu at (52.1, 86.4)
- added REF**: via-stitch, wr-efi:via-stitch, F.Cu at (55.9, 85.1)
- added REF**: via-stitch, wr-efi:via-stitch, F.Cu at (54.6, 85.1)
- added REF**: via-stitch, wr-efi:via-stitch, F.Cu at (53.3, 85.1)
- added REF**: via-stitch, wr-efi:via-stitch, F.Cu at (52.1, 85.1)
- added REF**: via-stitch, wr-efi:via-stitch, F.Cu at (55.9, 83.8)
- added REF**: via-stitch, wr-efi:via-stitch, F.Cu at (116.2, 59.7)
- added REF**: via-stitch, wr-efi:via-stitch, F.Cu at (54.6, 83.8)
- added REF**: via-stitch, wr-efi:via-stitch, F.Cu at (53.3, 83.8)
- added REF**: via-stitch, wr-efi:via-stitch, F.Cu at (52.1, 83.8)
- added REF**: via-stitch, wr-efi:via-stitch, F.Cu at (55.9, 82.5)
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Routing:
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
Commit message: more via stitch
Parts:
- added REF**: via-stitch, wr-efi:via-stitch, F.Cu at (95.2, 97.2)
- added REF**: via-stitch, wr-efi:via-stitch, F.Cu at (97.8, 92.1)
- added REF**: via-stitch, wr-efi:via-stitch, F.Cu at (99.1, 93.3)
- added REF**: via-stitch, wr-efi:via-stitch, F.Cu at (100.3, 94.6)
- added REF**: via-stitch, wr-efi:via-stitch, F.Cu at (96.5, 81.9)
- added REF**: via-stitch, wr-efi:via-stitch, F.Cu at (94.0, 81.9)
- added REF**: via-stitch, wr-efi:via-stitch, F.Cu at (94.6, 83.2)
- added REF**: via-stitch, wr-efi:via-stitch, F.Cu at (95.9, 84.5)
- added REF**: via-stitch, wr-efi:via-stitch, F.Cu at (97.2, 85.7)
- added REF**: via-stitch, wr-efi:via-stitch, F.Cu at (98.4, 87.0)
- added REF**: via-stitch, wr-efi:via-stitch, F.Cu at (99.7, 88.3)
- added REF**: via-stitch, wr-efi:via-stitch, F.Cu at (94.0, 95.9)
- added REF**: via-stitch, wr-efi:via-stitch, F.Cu at (101.0, 89.5)
- added REF**: via-stitch, wr-efi:via-stitch, F.Cu at (102.2, 90.8)
- added REF**: via-stitch, wr-efi:via-stitch, F.Cu at (103.5, 92.1)
- added REF**: via-stitch, wr-efi:via-stitch, F.Cu at (104.8, 93.3)
- added REF**: via-stitch, wr-efi:via-stitch, F.Cu at (106.0, 94.6)
- added REF**: via-stitch, wr-efi:via-stitch, F.Cu at (94.6, 86.4)
- added REF**: via-stitch, wr-efi:via-stitch, F.Cu at (95.9, 87.6)
- added REF**: via-stitch, wr-efi:via-stitch, F.Cu at (97.2, 88.9)
- added REF**: via-stitch, wr-efi:via-stitch, F.Cu at (98.4, 90.2)
- added REF**: via-stitch, wr-efi:via-stitch, F.Cu at (99.7, 91.4)
- added REF**: via-stitch, wr-efi:via-stitch, F.Cu at (94.0, 93.3)
- added REF**: via-stitch, wr-efi:via-stitch, F.Cu at (101.0, 92.7)
- added REF**: via-stitch, wr-efi:via-stitch, F.Cu at (102.2, 94.0)
- added REF**: via-stitch, wr-efi:via-stitch, F.Cu at (103.5, 95.2)
- added REF**: via-stitch, wr-efi:via-stitch, F.Cu at (101.6, 95.9)
- added REF**: via-stitch, wr-efi:via-stitch, F.Cu at (99.1, 95.9)
- added REF**: via-stitch, wr-efi:via-stitch, F.Cu at (97.8, 94.6)
- added REF**: via-stitch, wr-efi:via-stitch, F.Cu at (96.5, 93.3)
- added REF**: via-stitch, wr-efi:via-stitch, F.Cu at (95.2, 92.1)
- added REF**: via-stitch, wr-efi:via-stitch, F.Cu at (94.0, 90.8)
- added REF**: via-stitch, wr-efi:via-stitch, F.Cu at (122.6, 83.8)
- added REF**: via-stitch, wr-efi:via-stitch, F.Cu at (95.2, 94.6)
- added REF**: via-stitch, wr-efi:via-stitch, F.Cu at (122.6, 82.5)
- added REF**: via-stitch, wr-efi:via-stitch, F.Cu at (96.5, 95.9)
- added REF**: via-stitch, wr-efi:via-stitch, F.Cu at (97.8, 97.2)
- added REF**: via-stitch, wr-efi:via-stitch, F.Cu at (94.0, 88.3)
- added REF**: via-stitch, wr-efi:via-stitch, F.Cu at (95.2, 89.5)
- added REF**: via-stitch, wr-efi:via-stitch, F.Cu at (96.5, 90.8)
- moved REF** 0.64 mm to (92.7, 89.5)
- moved REF** 0.64 mm to (92.7, 94.6)
- moved REF** 0.64 mm to (93.3, 97.8)
- moved REF** 0.63 mm to (92.7, 92.1)
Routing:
- net +3V3: track 89.3 -> 88.3 mm, vias 15 -> 16
